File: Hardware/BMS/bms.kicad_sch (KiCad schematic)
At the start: 16 parts, among them SW1 SW_MEC_5E, SW2 SW_SPDT, U3 MAX33011EASA, U5 STM32G473CCTx, Y1 48 MHZ

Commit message: edits to the BMS
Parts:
- added J101: Conn_01x02, Connector_Molex:Molex_Nano-Fit_105313-xx02_1x02_P2.50mm_Horizontal, symbol Connector_Generic:Conn_01x02
- added J102: Conn_02x05_Top_Bottom, Connector_Molex:Molex_Micro-Fit_3.0_43045-1000_2x05_P3.00mm_Horizontal, symbol Connector_Generic:Conn_02x05_Top_Bottom
- added J103: Conn_02x02_Counter_Clockwise, Connector_Molex:Molex_Micro-Fit_3.0_43045-0400_2x02_P3.00mm_Horizontal, symbol Connector_Generic:Conn_02x02_Counter_Clockwise
- added R103: 5k, OEM:R_0603_1608Metric, symbol OEM:1KR
- added R104: 330, OEM:R_0603_1608Metric, symbol OEM:1KR
- added U103: LTV-356T, Package_SO:SO-4_4.4x3.6mm_P2.54mm, symbol Isolator:LTV-356T
- renumbered C15 to C101, C22 to C102, C23 to C103, C24 to C104, C25 to C105, C26 to C106, C27 to C107, C28 to C108, C29 to C109, R31 to R101, R36 to R102, SW1 to SW101, SW2 to SW102, U3 to U101, U5 to U102, Y1 to Y101
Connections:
- net +3.3V: now also R103.1
- net GND: now also J101.2 (Pin_2), J102.10 (Pin_10), J103.2 (Pin_2), U103.2
- net I2C2_SCL: no longer U102.30 (PA8)
- net at U102.45 (PB8): no longer R102.2
- new net: R104.2, U103.1
- new net +BATT: J102.5 (Pin_5)
- new net BMS_EN: J102.9 (Pin_9)
- new net BMS_OK: R104.1
- new net BMS_SD+: J102.3 (Pin_3), U103.4
- new net BMS_SD-: J102.4 (Pin_4), U103.3
- new net BMS_SDO: R103.2
- new net BREAKER_EN: J101.1 (Pin_1)
- new net CAN+: J102.1 (Pin_1), J102.6 (Pin_6)
- new net CAN-: J102.2 (Pin_2), J102.7 (Pin_7)
- new net I2C2_SDA: U102.30 (PA8)
- new net I_SENSE_+: J103.4 (Pin_4)
- new net I_SENSE_-: J103.3 (Pin_3)
- new net THERM_BUSBAR: J103.1 (Pin_1)
- no-connect marks 1 -> 2
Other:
- removed sheet ADBMS
- added sheet ADBMS1818 (ADBMS1818.kicad_sch)
- added sheet Power (power.kicad_sch)
- sheet Thermistors ports: added +3.3V, SCL, SDA, THERM_BUSBAR; removed I2C1_SCL, I2C1_SDA, I2C2_SCL, I2C2_SDA
- note added: "Breaker Connection"
- moved on the sheet: C102, C103, C104, C105, C106, C107, C108, C109, R102, SW101, SW102, U102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

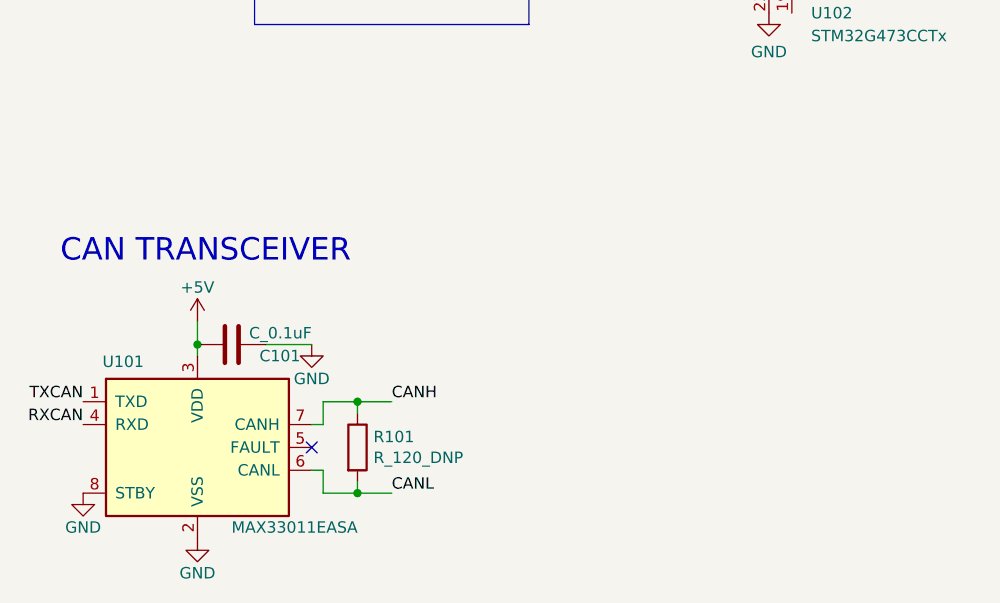
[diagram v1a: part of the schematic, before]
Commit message: added can transciever
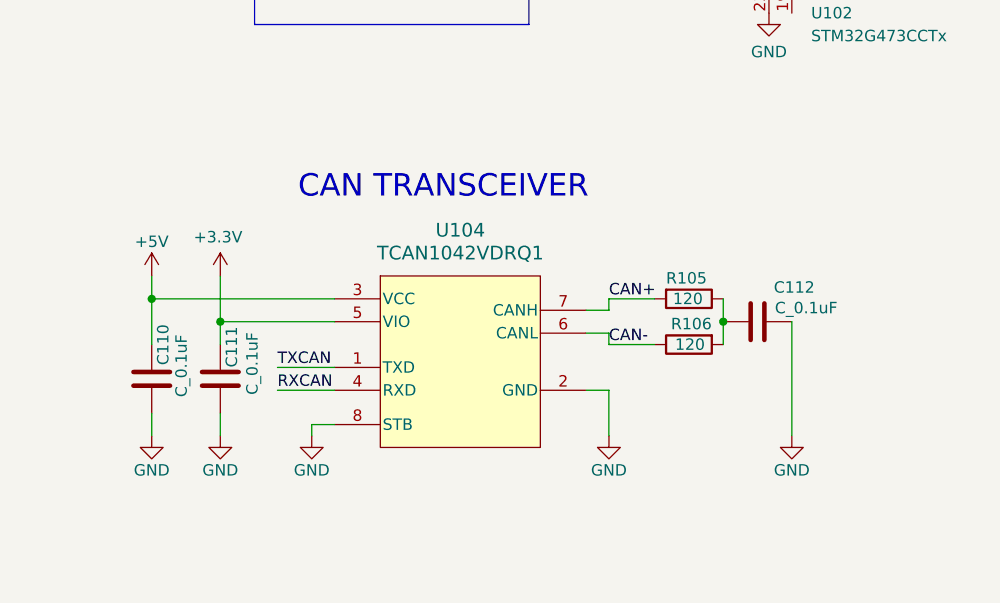
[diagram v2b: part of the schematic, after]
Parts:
- removed C101: C_0.1uF, OEM:C_0603_1608Metric, symbol OEM:0u1F
- removed R101: R_120_DNP, OEM:R_0603_1608Metric, symbol OEM:120R_DNP
- removed U101: MAX33011EASA, OEM:SOIC-8_3.9x4.9mm_Pitch1.27mm_OEM, symbol OEM:MAX33011EASA
- added C110, C111, C112: C_0.1uF, OEM:C_0603_1608Metric, symbol OEM:0u1F
- added R105, R106: 120, OEM:R_0603_1608Metric, symbol OEM:120R_DNP
- added U104: TCAN1042VDRQ1, BAD_LIB:D0008A_M, symbol OlinBAD:TCAN1042VDRQ1
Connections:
- net +3.3V: now also C111.1, U104.5 (VIO)
- net +5V: now also C110.1, U104.3 (VCC)
- net CAN+: now also R105.2, U104.7 (CANH)
- net CAN-: now also R106.1, U104.6 (CANL)
- net GND: now also C110.2, C111.2, C112.2, U104.2 (GND), U104.8 (STB)
- net RXCAN: now also U104.4 (RXD)
- net TXCAN: now also U104.1 (TXD)
- new net: C112.1, R105.1, R106.2
- no-connect marks 2 -> 1
